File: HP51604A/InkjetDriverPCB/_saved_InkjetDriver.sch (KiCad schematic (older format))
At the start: 17 parts, among them P1 EXPANSION_HEADER, P2 PWR, P3 INKJET, U1 6B595, U2 6B595, U3 LT1072

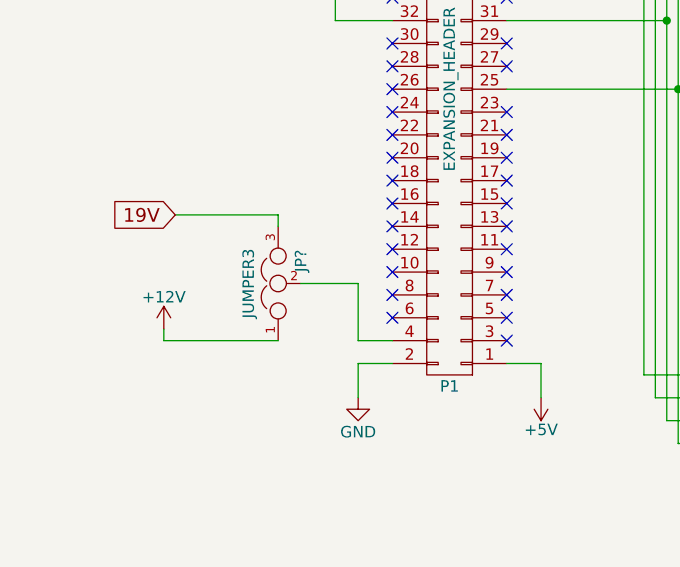
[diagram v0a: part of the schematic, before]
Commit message: Interface PCB changed to allow 19V supply to be routed past the buck converter.
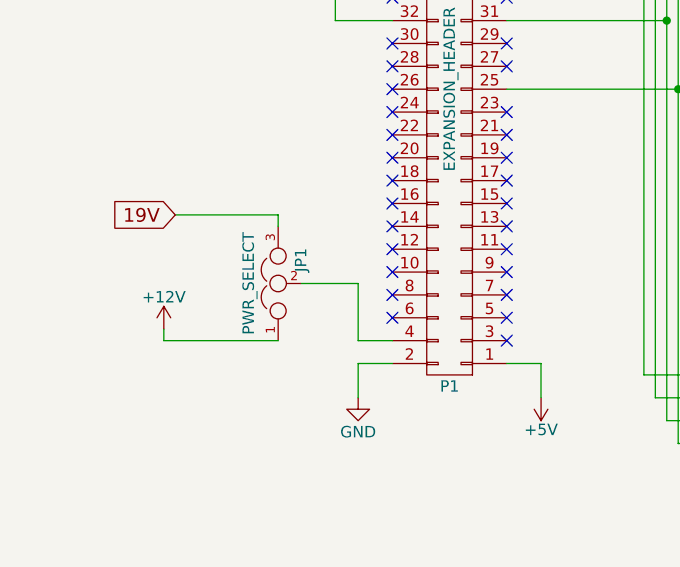
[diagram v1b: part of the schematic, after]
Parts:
- JP1: renamed from JP?; value JUMPER3 -> PWR_SELECT; footprint (none) -> Socket_Strips:Socket_Strip_Straight_1x03
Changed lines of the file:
@@
 	1300 3100 1750 3100
 $Comp
-L JUMPER3 JP?
+L JUMPER3 JP1
 U 1 1 55A3EE6A
 P 1750 3400
-F 0 "JP?" H 1800 3300 50  0000 L CNN
-F 1 "JUMPER3" H 1750 3500 50  0000 C BNN
-F 2 "" H 1750 3400 60  0000 C CNN
+F 0 "JP1" H 1800 3300 50  0000 L CNN
+F 1 "PWR_SELECT" H 1750 3500 50  0000 C BNN
+F 2 "Socket_Strips:Socket_Strip_Straight_1x03" H 1750 3400 60  0001 C CNN
 F 3 "" H 1750 3400 60  0000 C CNN
 	1    1750 3400
